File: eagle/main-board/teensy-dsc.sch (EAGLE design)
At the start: 29 parts, among them J1 RJ11-6PTH, J2 RJ11-6PTH, J3 RJ45-8PTH, J4 POWER_JACKPTH, J5 USB-B, Q1 IRLML6344, X1 STEREOJACK, X2 STEREOJACK

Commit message: Initial WizFi210/220 redesign
Also fixes naming of various Teensy pins which were wrong
or incorrectly routed for serial ports/shutter/focus per
the Google doc.
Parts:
- U$5: value XBEERX-VN -> (none); device xbee_r1:XBEERX-VN -> WizFi210:WIZFI210/220
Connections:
- net P14 renamed LCD_DC
- net P15 renamed LCD_CS
- net P24 renamed TEMP
- net P25 renamed C1
- net P26 renamed C2
- net P27 renamed D1
- net P28 renamed D2
- net P29 renamed C_BUTTON
- net P30 renamed D_BUTTON
- net P31 renamed BATTMON
- net P33 renamed LCD_RESET
- removed net AGND: JP2.4, U$1.AGND
- removed net AREF: JP2.3, U$1.AREF
- removed net FOCUS-CTL: U$1.20/A6/PWM, U$6A.A
- removed net P11: JP1.14, U$1.11/MOSI
- removed net P12: JP1.13, U$1.12/MISO
- removed net P13: JP1.12, U$1.13/SCK/LED
- removed net P16: JP1.9, U$1.16/A2/T
- removed net P17: JP1.8, U$1.17/A3/T
- removed net P18: JP1.7, U$1.18/A4/T/SDA0
- removed net P19: JP1.6, U$1.19/A5/T/SCL0
- removed net P2: JP1.15, U$1.2
- removed net PGM: JP2.2, U$1.PGM
- removed net SHUTTER-CTL: U$1.21/A7/PWM, U$6B.A
- removed net XBEE_IN: U$1.8/TX3, U$5.DIN
- removed net XBEE_OUT: U$1.7/RX3, U$5.DOUT
- removed net XBEE_RST: U$1.A14/DAC, U$5.RESET#
- new net DEW1: JP1.9, U$1.20/A6/PWM
- new net DEW2: JP1.8, U$1.21/A7/PWM
- new net DEW3: JP1.7, U$1.22/A8/T/PWM
- new net DEW4: JP1.6, U$1.23/A9/T/PWM
- new net FOCUS_CTL: U$1.16/A2/T, U$6A.A
- new net MISO: JP1.13, U$1.12/MISO, U$5.SSPI_MISO
- new net MOSI: JP1.14, U$1.11/MOSI, U$5.SSPI_MOSI
- new net RX3: JP1.16, U$1.7/RX3
- new net SCK: JP1.12, U$1.13/SCK/LED, U$5.SSPI_CLK
- new net SHUTTER_CTL: U$1.17/A3/T, U$6B.A
- new net TX3: JP1.15, U$1.8/TX3
- new net WIZNET_CS: U$1.2, U$5.SSPI_CS
- new net WIZNET_FACRESET: U$1.A14/DAC, U$5.GPIO21_CLK-11M
- net 3.3V: now also U$5.EN_1V8, U$5.VBAT, U$5.VDDIO, U$5.VIN_3V3; no longer U$5.VCC@1
- net 5V: now also JP2.2; no longer JP1.16
- net GND: now also U$5.GND@1, U$5.GND@2, U$5.GND@3, U$5.GND@4; no longer U$5.GND@10
- net SW1: now also U$1.18/A4/T/SDA0; no longer U$1.22/A8/T/PWM
- net SW2: now also U$1.19/A5/T/SCL0; no longer U$1.23/A9/T/PWM
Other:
- moved on the sheet: J1, J2, R1, R2, U$6A, U$6B

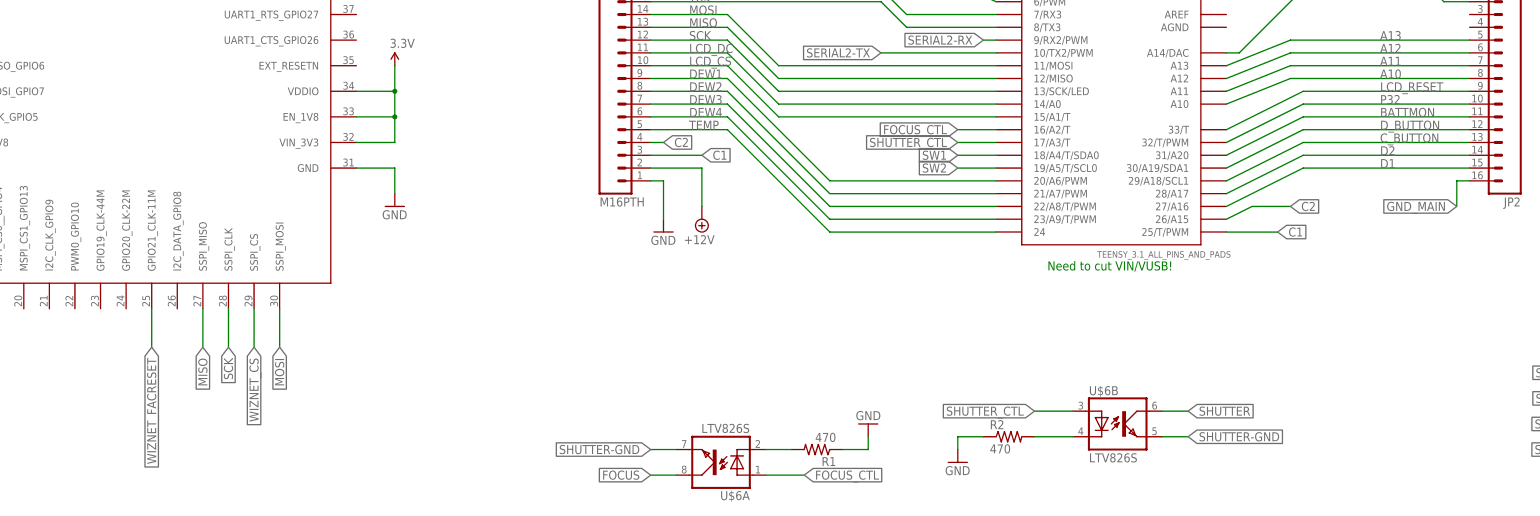
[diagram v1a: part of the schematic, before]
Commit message: more WizFi updates....
After further research, I'm not convinced the WizFi is the way to go.
Most likely will need to replace it with something else if I want
to support serial ports.  Probably should move the serial ports
to a daughter board.
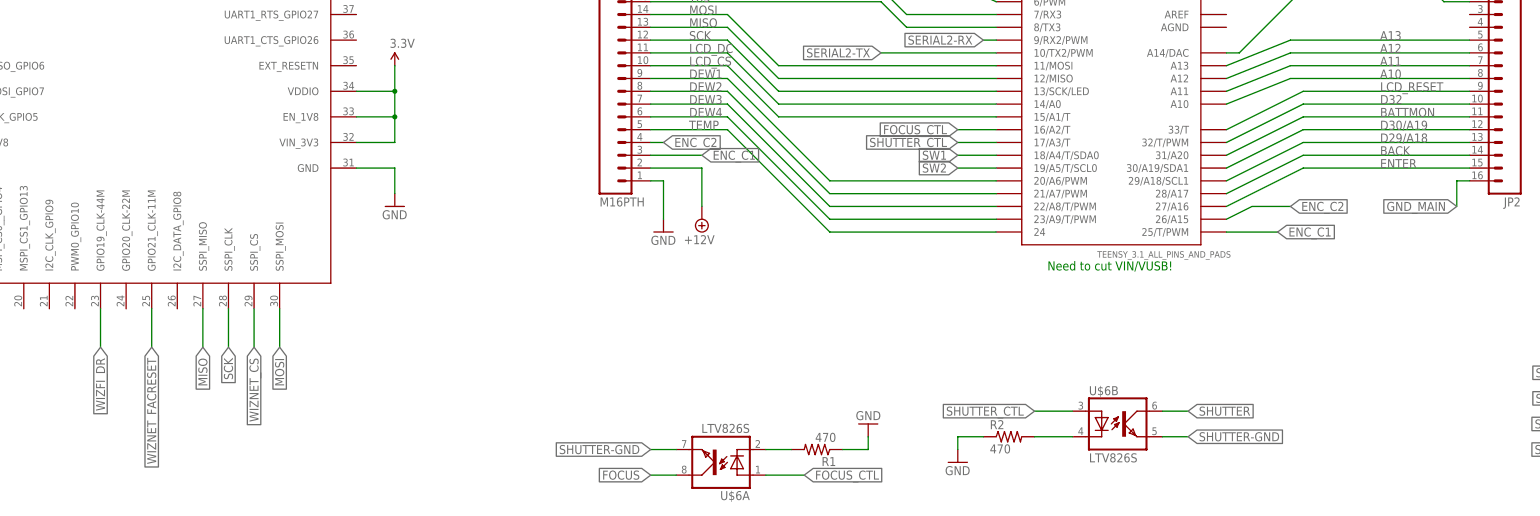
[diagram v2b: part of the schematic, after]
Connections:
- net C1 renamed ENC_C1
- net C2 renamed ENC_C2
- net C_BUTTON renamed D29/A18
- net D1 renamed ENTER
- net D2 renamed BACK
- net D_BUTTON renamed D30/A19
- net P32 renamed D32
- new net WIZFI_DR: U$5.GPIO19_CLK-44M
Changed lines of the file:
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@@
 </segment>
 </net>
-<net name="P32" class="0">
+<net name="D32" class="0">
 <segment>
 <pinref part="U$1" gate="G$1" pin="32/T/PWM"/>
@@
 </segment>
 </net>
-<net name="D_BUTTON" class="0">
+<net name="D30/A19" class="0">
 <segment>
 <pinref part="U$1" gate="G$1" pin="30/A19/SDA1"/>
@@
 </segment>
 </net>
-<net name="C_BUTTON" class="0">
+<net name="D29/A18" class="0">
 <segment>
 <pinref part="U$1" gate="G$1" pin="29/A18/SCL1"/>
@@
 </segment>
 </net>
-<net name="D2" class="0">
+<net name="BACK" class="0">
 <segment>
 <pinref part="U$1" gate="G$1" pin="28/A17"/>
@@
 <wire x1="99.06" y1="45.72" x2="132.08" y2="45.72" width="0.1524" layer="91"/>
 <label x="114.3" y="45.72" size="1.778" layer="95"/>
-</segment>
-</net>
-<net name="D1" class="0">
-<segment>
-<pinref part="U$1" gate="G$1" pin="27/A16"/>
-<pinref part="JP2" gate="G$1" pin="15"/>
-<wire x1="83.82" y1="35.56" x2="99.06" y2="43.18" width="0.1524" layer="91"/>
-<wire x1="99.06" y1="43.18" x2="132.08" y2="43.18" width="0.1524" layer="91"/>
-<label x="114.3" y="43.18" size="1.778" layer="95"/>
 </segment>
 </net>
@@
 </segment>
 </net>
-<net name="C1" class="0">
+<net name="ENC_C1" class="0">
 <segment>
 <pinref part="JP1" gate="G$1" pin="3"/>
@@
 </segment>
 </net>
-<net name="C2" class="0">
+<net name="ENC_C2" class="0">
 <segment>
 <pinref part="JP1" gate="G$1" pin="4"/>
@@
 </segment>
 </net>
+<net name="ENTER" class="0">
+<segment>
+<pinref part="U$1" gate="G$1" pin="27/A16"/>
+<pinref part="JP2" gate="G$1" pin="15"/>
+<wire x1="83.82" y1="35.56" x2="99.06" y2="43.18" width="0.1524" layer="91"/>
+<wire x1="99.06" y1="43.18" x2="132.08" y2="43.18" width="0.1524" layer="91"/>
+<label x="114.3" y="43.18" size="1.778" layer="95"/>
+</segment>
+</net>
+<net name="WIZFI_DR" class="0">
+<segment>
+<pinref part="U$5" gate="G$1" pin="GPIO19_CLK-44M"/>
+<wire x1="-139.7" y1="15.24" x2="-139.7" y2="7.62" width="0.1524" layer="91"/>
+<label x="-139.7" y="7.62" size="1.778" layer="95" rot="R270" xref="yes"/>
+</segment>
+</net>
